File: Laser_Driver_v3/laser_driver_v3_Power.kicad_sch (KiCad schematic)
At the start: 0 parts

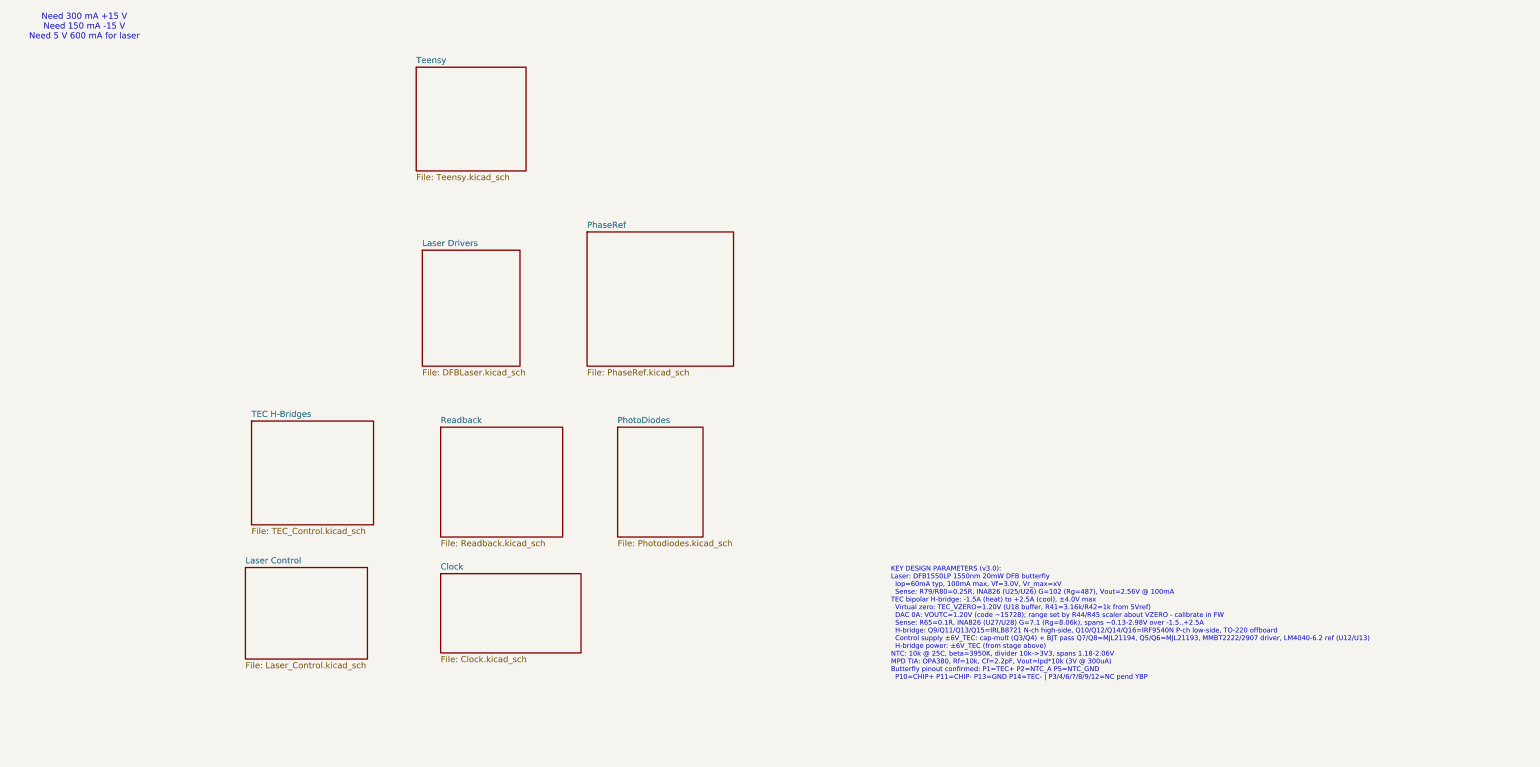
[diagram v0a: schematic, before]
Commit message: Split into a power and signal board.
I think all footprints are now valid.  Need to figure out the power connections between boards, currently just screw terminals for wire.  I think a single multi-pin connector will work, but want to find something with premade off the shelf cables.
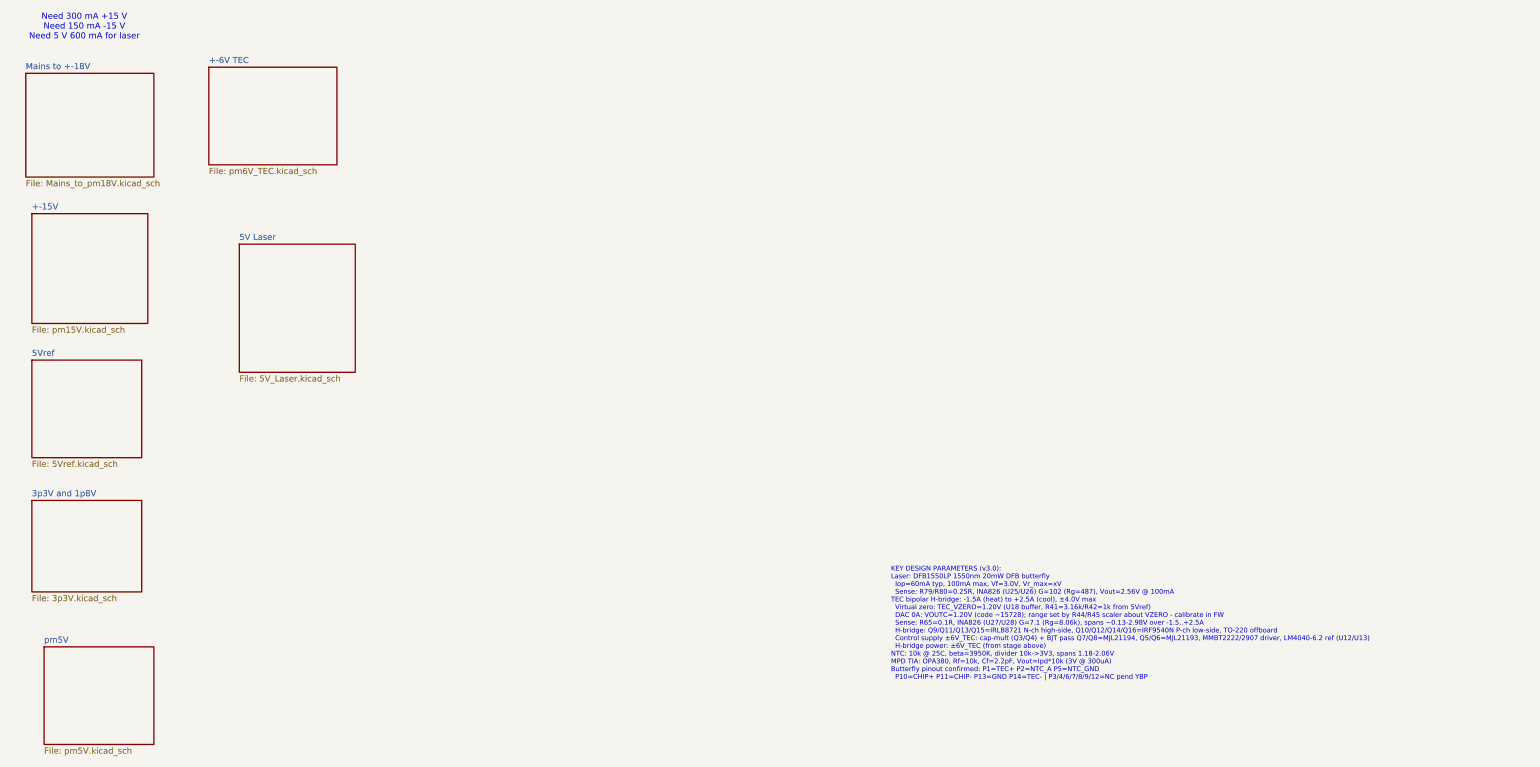
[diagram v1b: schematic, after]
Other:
- removed sheet Clock
- removed sheet Laser Control
- removed sheet Laser Drivers
- removed sheet PhaseRef
- removed sheet PhotoDiodes
- removed sheet Readback
- removed sheet TEC H-Bridges
- removed sheet Teensy
- added sheet +-15V (pm15V.kicad_sch)
- added sheet +-6V TEC (pm6V_TEC.kicad_sch)
- added sheet 3p3V and 1p8V (3p3V.kicad_sch)
- added sheet 5V Laser (5V_Laser.kicad_sch)
- added sheet 5Vref (5Vref.kicad_sch)
- added sheet Mains to +-18V (Mains_to_pm18V.kicad_sch)
- added sheet pm5V (pm5V.kicad_sch)

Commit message: First power pcb layout without traces.
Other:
- added sheet PowerConnectorOut (PowerConnector.kicad_sch)
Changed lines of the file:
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@@
+	)
+	(sheet
+		(at 66.04 101.6)
+		(size 22.86 25.4)
+		(exclude_from_sim no)
+		(in_bom yes)
+		(on_board yes)
+		(dnp no)
+		(fields_autoplaced yes)
+		(stroke
+			(width 0.1524)
+			(type solid)
+		)
+		(fill
+			(color 0 0 0 0)
+		)
+		(property "Sheetname" "PowerConnectorOut"
+			(at 66.04 100.8884 0)
+			(show_name no)
+			(do_not_autoplace no)
+			(effects
+				(font
+					(size 1.27 1.27)
+				)
+				(justify left bottom)
+			)
+		)
+		(property "Sheetfile" "PowerConnector.kicad_sch"
+			(at 66.04 127.5846 0)
+			(show_name no)
+			(do_not_autoplace no)
+			(effects
+				(font
+					(size 1.27 1.27)
+				)
+				(justify left top)
+			)
+		)
+		(instances
+			(project "laser_driver_v3_Power"
+				(path "/b2c3d4e5-f6a7-8901-bcde-f12345678901"
+					(page "8")
+				)
+			)
+		)
 	)
 	(sheet

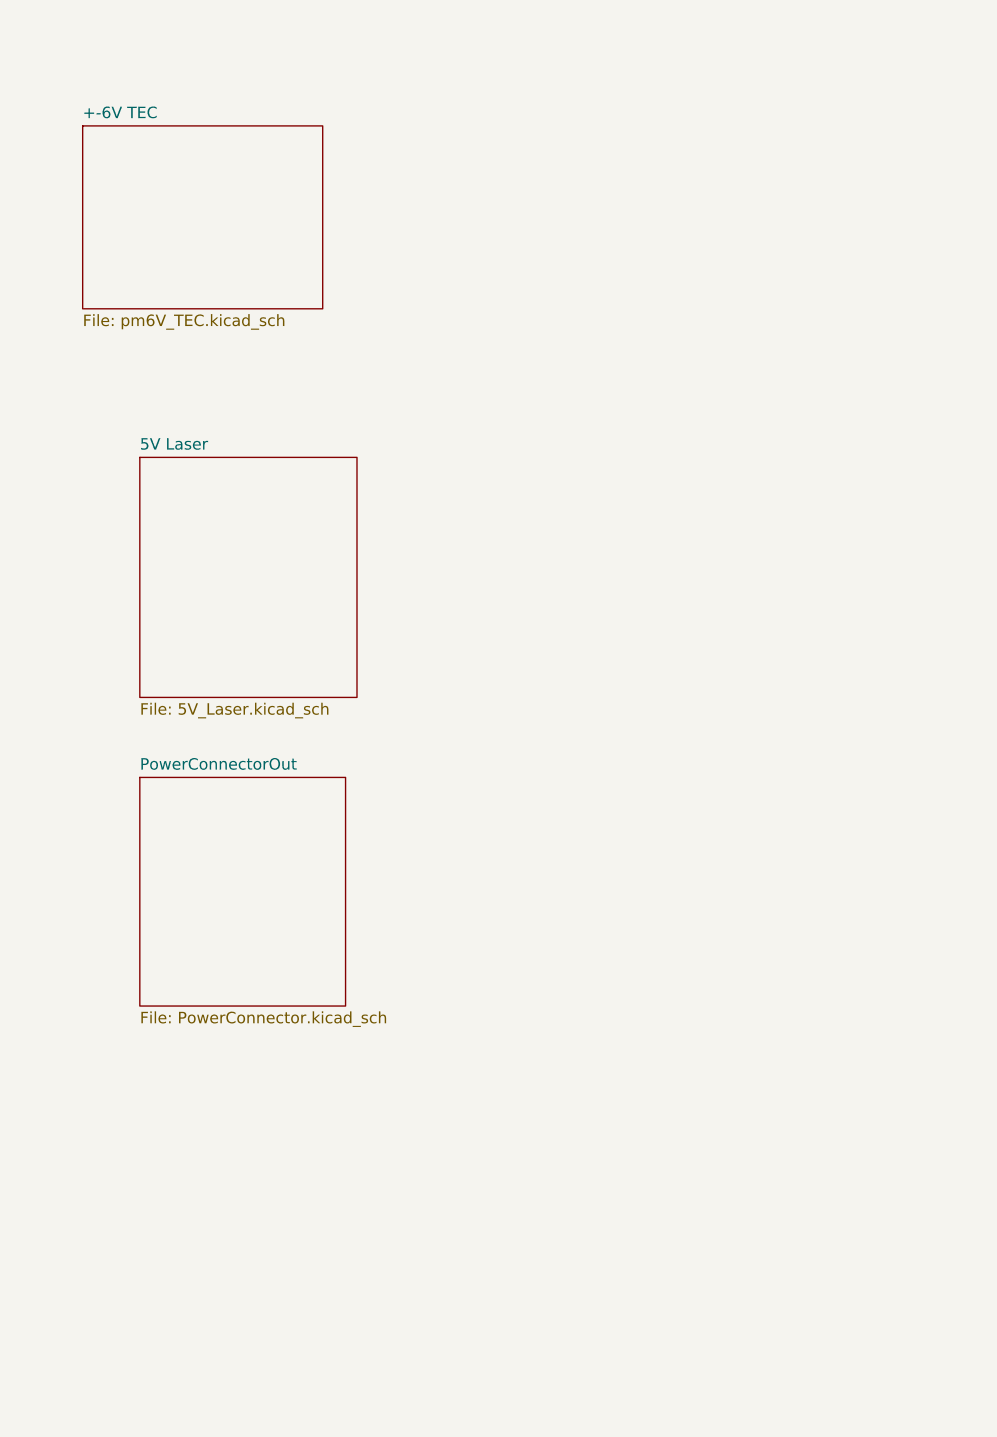
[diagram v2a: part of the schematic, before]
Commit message: Adding rail voltage good led circuitry.
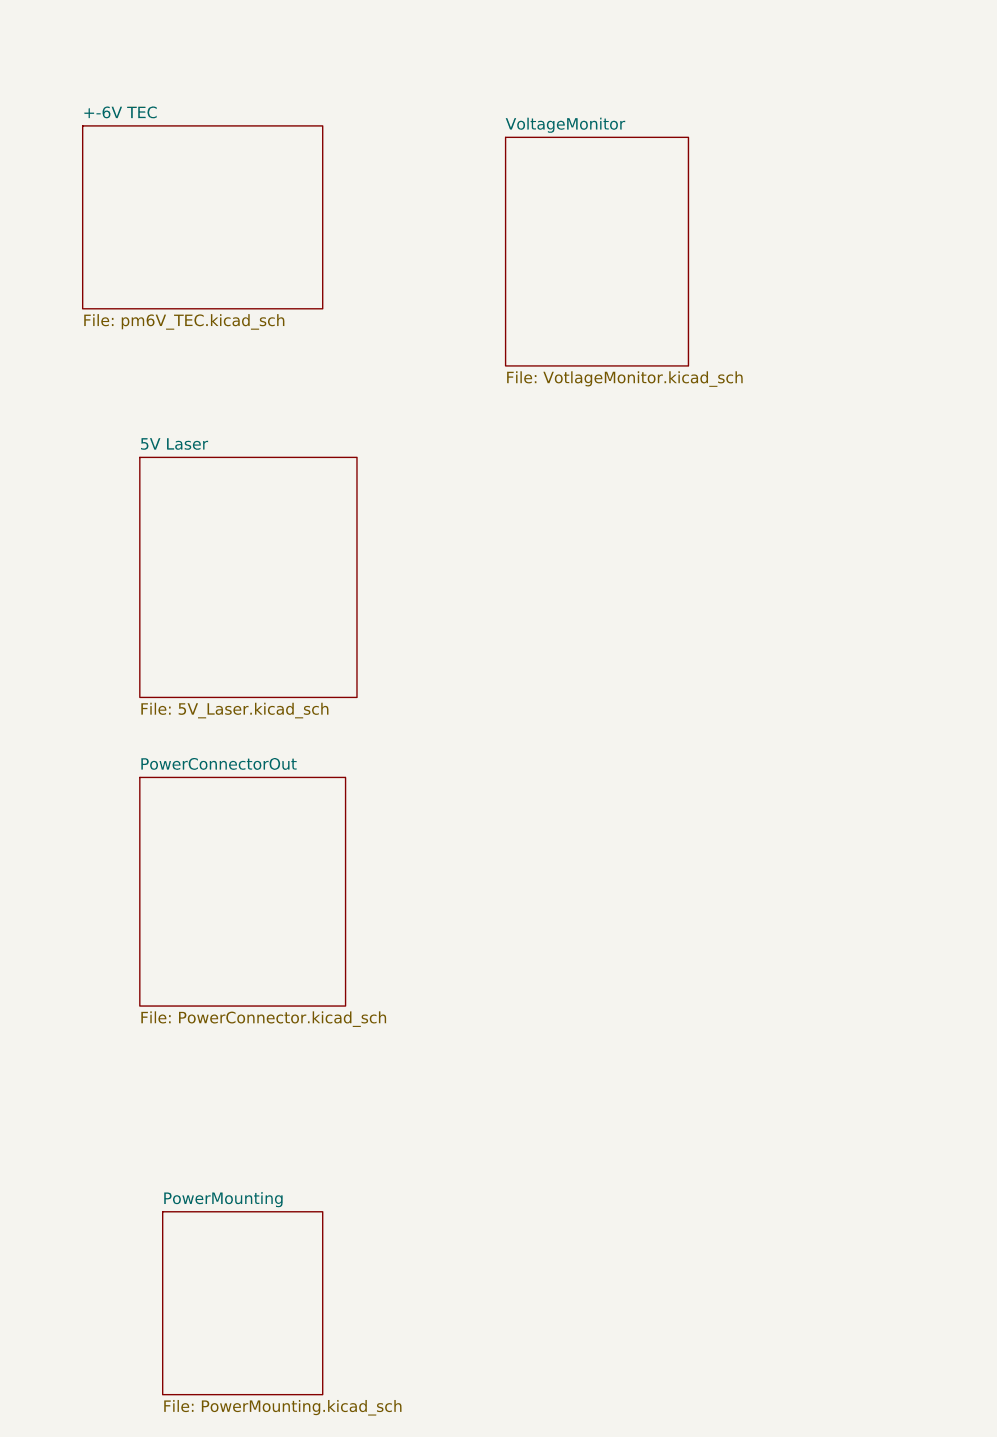
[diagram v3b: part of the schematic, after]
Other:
- added sheet PowerMounting (PowerMounting.kicad_sch)
- added sheet VoltageMonitor (VotlageMonitor.kicad_sch)
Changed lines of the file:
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@@
+		)
+	)
+	(sheet
+		(at 68.58 149.86)
+		(size 17.78 20.32)
+		(exclude_from_sim no)
+		(in_bom yes)
+		(on_board yes)
+		(dnp no)
+		(fields_autoplaced yes)
+		(stroke
+			(width 0.1524)
+			(type solid)
+		)
+		(fill
+			(color 0 0 0 0)
+		)
+		(property "Sheetname" "PowerMounting"
+			(at 68.58 149.1484 0)
+			(show_name no)
+			(do_not_autoplace no)
+			(effects
+				(font
+					(size 1.27 1.27)
+				)
+				(justify left bottom)
+			)
+		)
+		(property "Sheetfile" "PowerMounting.kicad_sch"
+			(at 68.58 170.7646 0)
+			(show_name no)
+			(do_not_autoplace no)
+			(effects
+				(font
+					(size 1.27 1.27)
+				)
+				(justify left top)
+			)
+		)
+		(instances
+			(project "laser_driver_v3_Power"
+				(path "/b2c3d4e5-f6a7-8901-bcde-f12345678901"
+					(page "9")
+				)
+			)
+		)
+	)
+	(sheet
+		(at 106.68 30.48)
+		(size 20.32 25.4)
+		(exclude_from_sim no)
+		(in_bom yes)
+		(on_board yes)
+		(dnp no)
+		(fields_autoplaced yes)
+		(stroke
+			(width 0.1524)
+			(type solid)
+		)
+		(fill
+			(color 0 0 0 0)
+		)
+		(property "Sheetname" "VoltageMonitor"
+			(at 106.68 29.7684 0)
+			(show_name no)
+			(do_not_autoplace no)
+			(effects
+				(font
+					(size 1.27 1.27)
+				)
+				(justify left bottom)
+			)
+		)
+		(property "Sheetfile" "VotlageMonitor.kicad_sch"
+			(at 106.68 56.4646 0)
+			(show_name no)
+			(do_not_autoplace no)
+			(effects
+				(font
+					(size 1.27 1.27)
+				)
+				(justify left top)
+			)
+		)
+		(instances
+			(project "laser_driver_v3_Power"
+				(path "/b2c3d4e5-f6a7-8901-bcde-f12345678901"
+					(page "10")
+				)
+			)
 		)
 	)
